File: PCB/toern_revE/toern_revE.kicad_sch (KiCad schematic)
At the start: 81 parts, among them J1 AudioJack3_Switch, J11 Conn_01x05, J11.5 Conn_01x05, J12 Conn_01x05, J13 Conn_01x05, J14 Conn_01x05, J15 Conn_01x05, J16 BATTERY, J2 CUI_SJ2-35863B1-SMT-TR, J3 CUI_SJ2-35863B1-SMT-TR, J4 USB_C_Receptacle_USB2.0, J5 AudioJack3_Switch, J6 AudioJack3_Switch, J7 AudioJack3_Switch, J8 Micro_SD_Card, J9 Conn_01x03, Q1 DMG3415, SW1 EG2219, U1 SPX3819M5-L-3-3, U10 01x05 Connector_PinSocket_2.5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, U11 01x05 Connector_PinSocket_2.5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, U12 01x05 Connector_PinSocket_2.5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, U13 01x05 Connector_PinSocket_2.5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, U14 01x05 Connector_PinSocket_2.5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, U15 01x05 Connector_PinSocket_2.5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, U16 01x05 Connector_PinSocket_2.5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, U2 SPX3819M5-L-1-8, U3 SGTL5000XNBA3, U4 TLP2361V4_E, U5 74LVC2G14, U6 Teensy4.1, U7 SPX3819M5-L-3-3, U8 MCP73831-3-OT, U9 01x05 Connector_PinSocket_2.5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

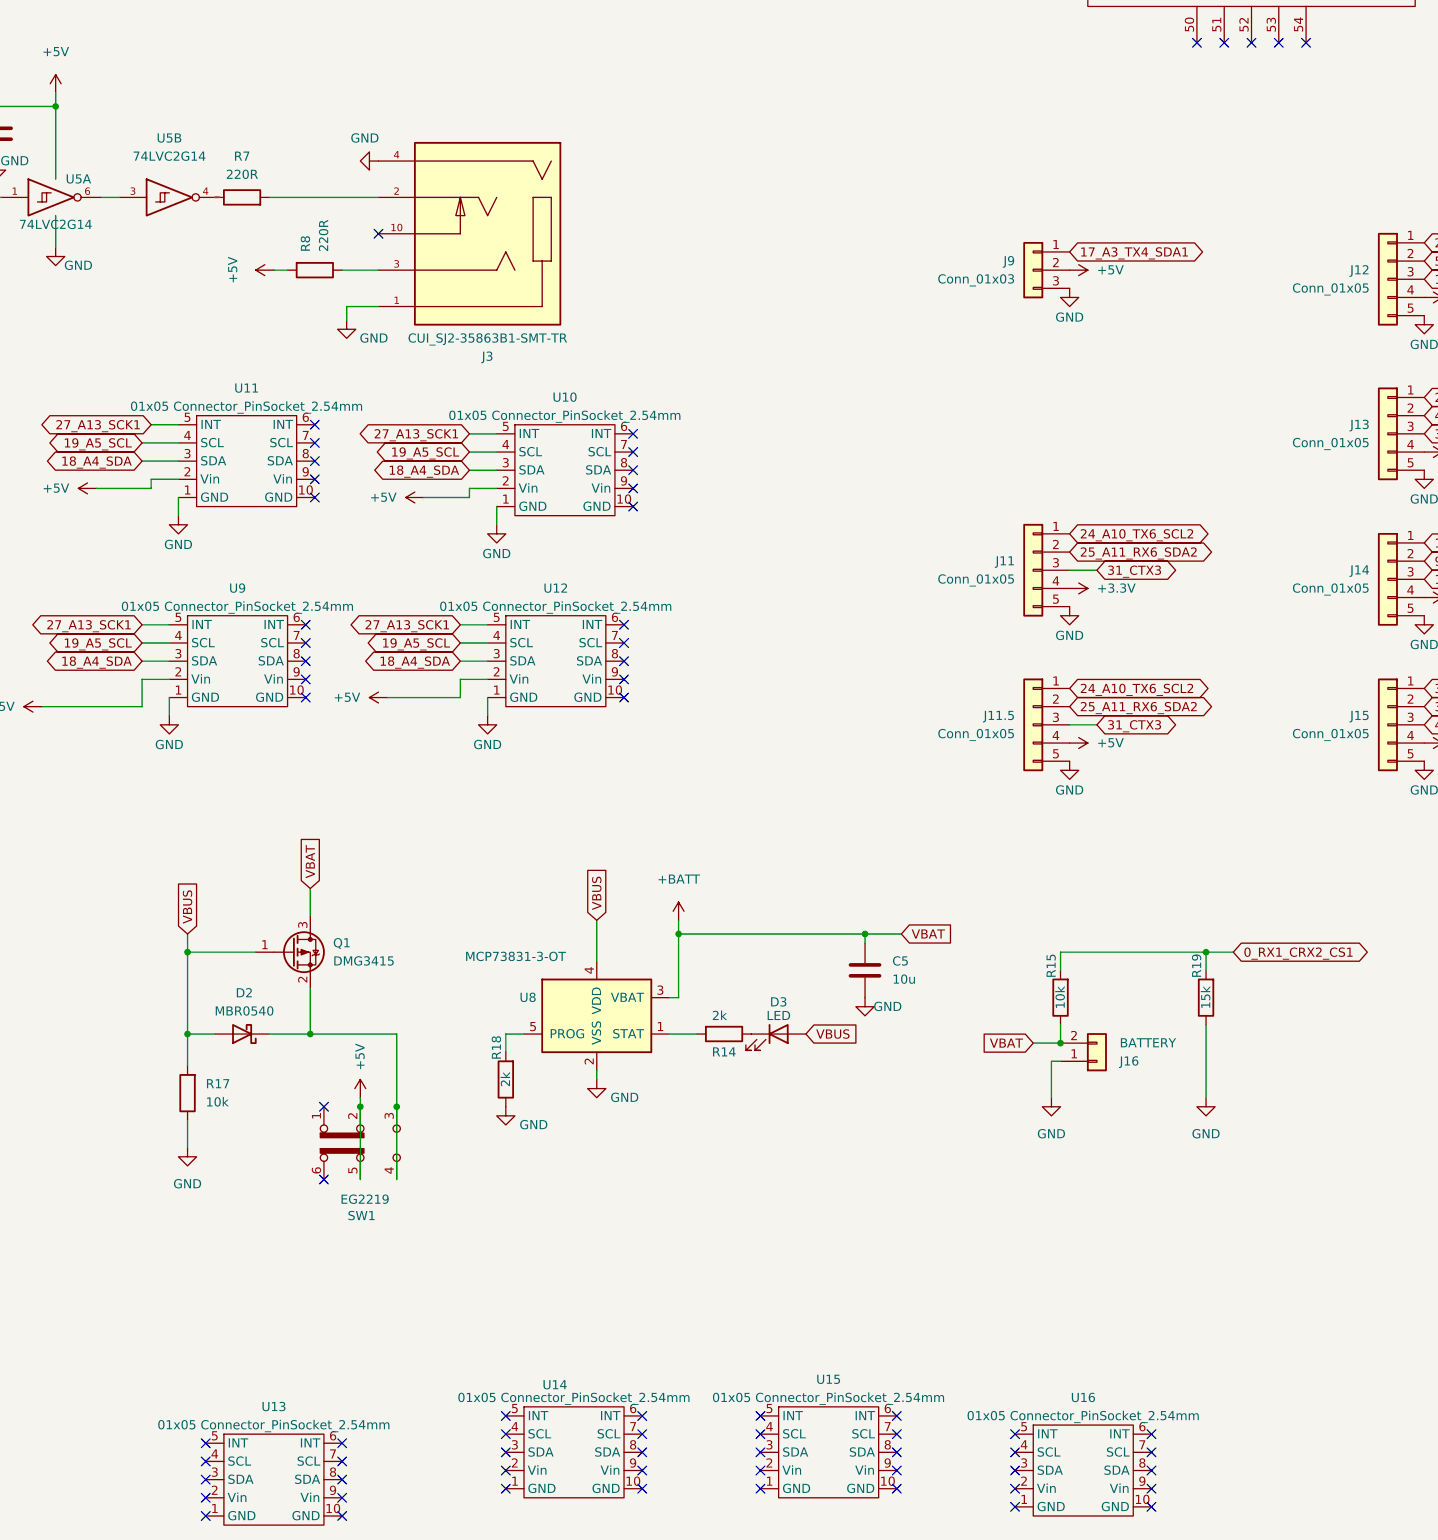
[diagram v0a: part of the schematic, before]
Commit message: varoious fixes in stability
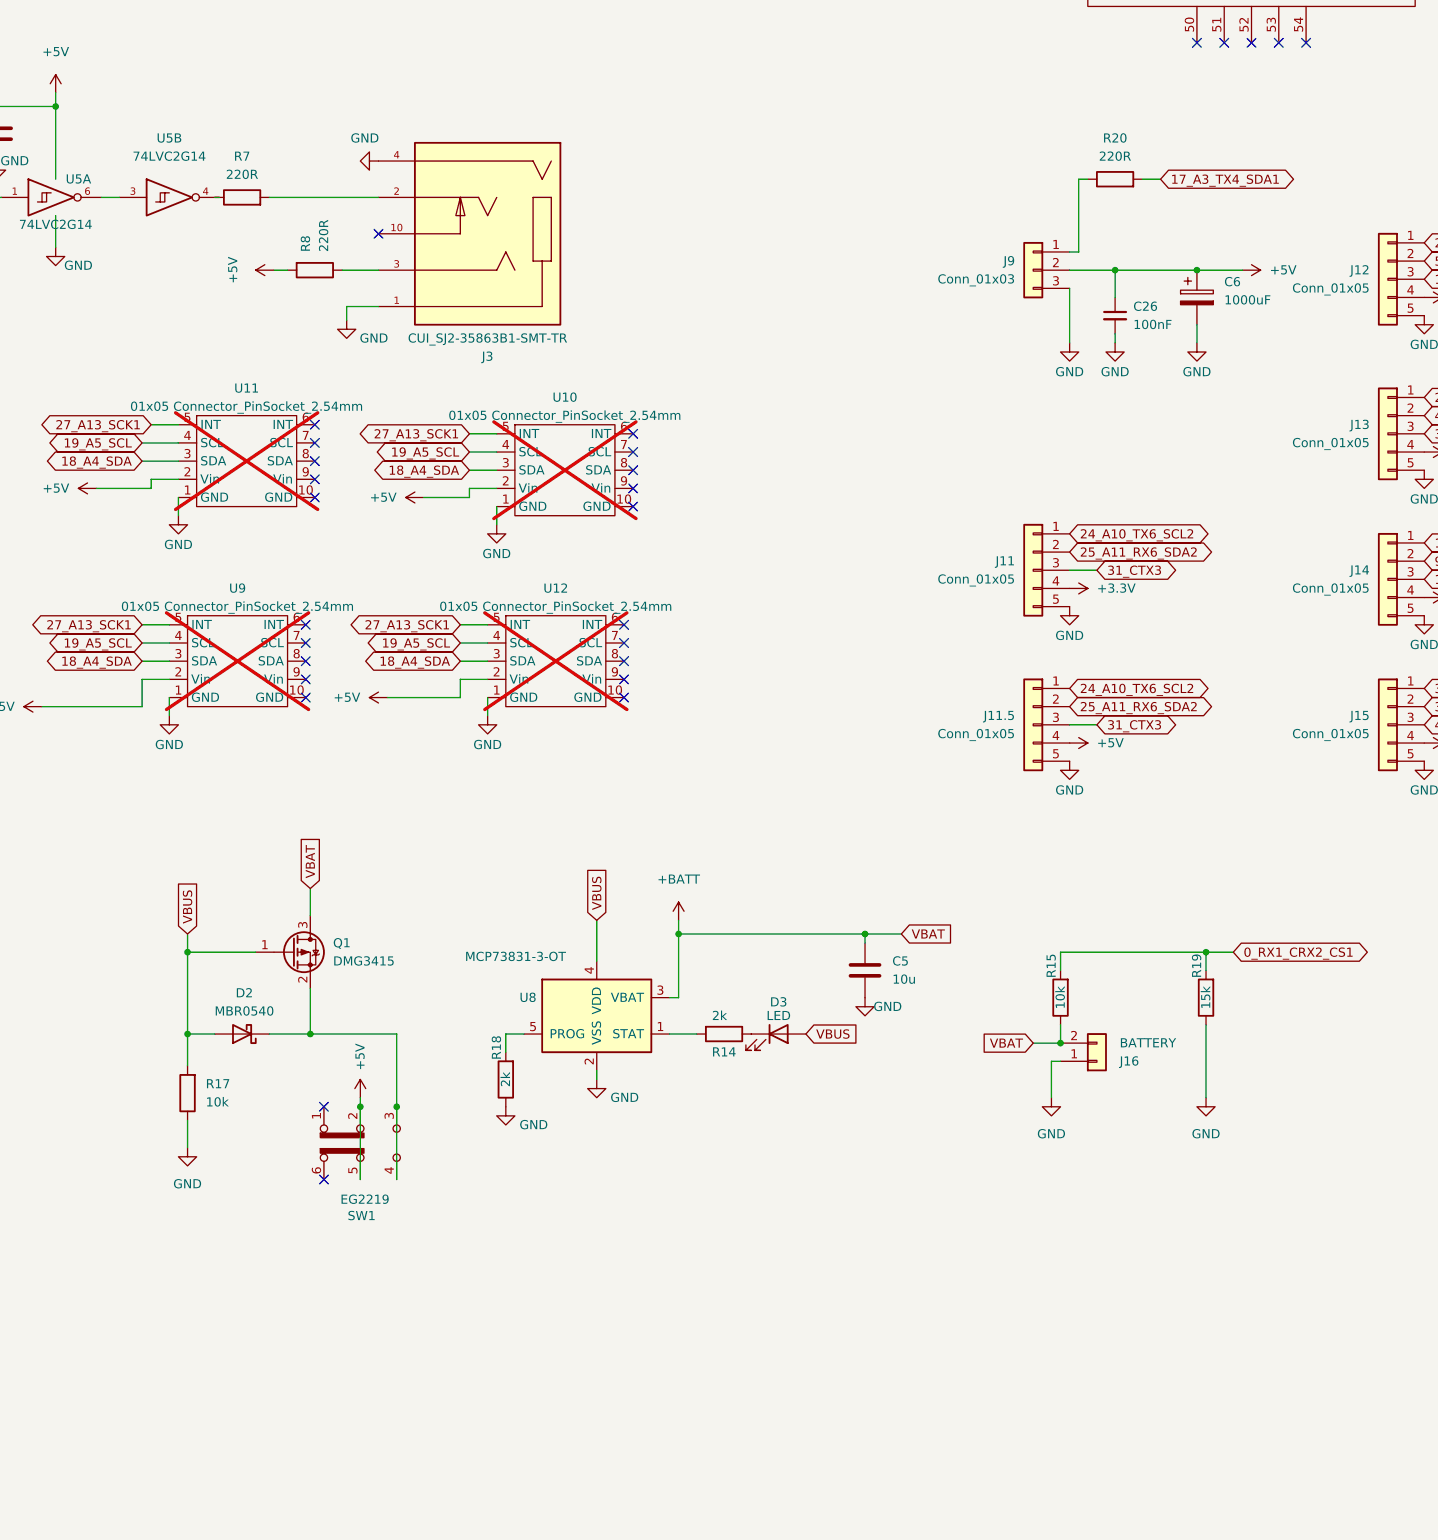
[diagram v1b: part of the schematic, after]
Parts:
- removed U13, U14, U15, U16: 01x05 Connector_PinSocket_2.54mm, Connector_PinSocket_2.54mm:DuppaI2CEncoderV2.1, symbol Connector:DuppaI2C
- added C26: 100nF, Capacitor_SMD:C_0805_2012Metric, symbol Device:C_Small
- added C6: 1000uF, Capacitor_SMD:CP_Elec_8x10.5, symbol Device:C_Polarized
- added R20: 220R, Resistor_SMD:R_0603_1608Metric, symbol Device:R
- U10, U11, U12, U9: now not fitted
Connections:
- net +5V: now also C26.1, C6.1
- net 17_A3_TX4_SDA1: now also R20.2; no longer J9.1 (Pin_1)
- net GND: now also C26.2, C6.2
- new net: J9.1 (Pin_1), R20.1
- no-connect marks 102 -> 62
